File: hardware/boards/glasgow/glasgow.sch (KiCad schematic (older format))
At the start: 80 parts, among them J1 USB_B_Micro, U1 CY7C68013A-56LTX, U15 TPD3S014, U2 CAT24M01W, U3 CAT24C256W, U30 ICE40HX8K-BG121, U34 ATECC508A, U7 LM3880MF-1AF, U8 MIC5355-S4YMME, Y1 24M

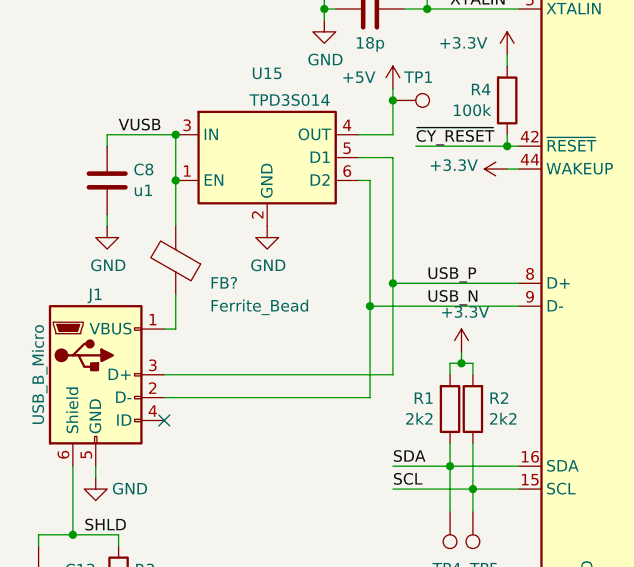
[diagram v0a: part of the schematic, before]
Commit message: Added 1BitSquared BOM keys to the schematic.
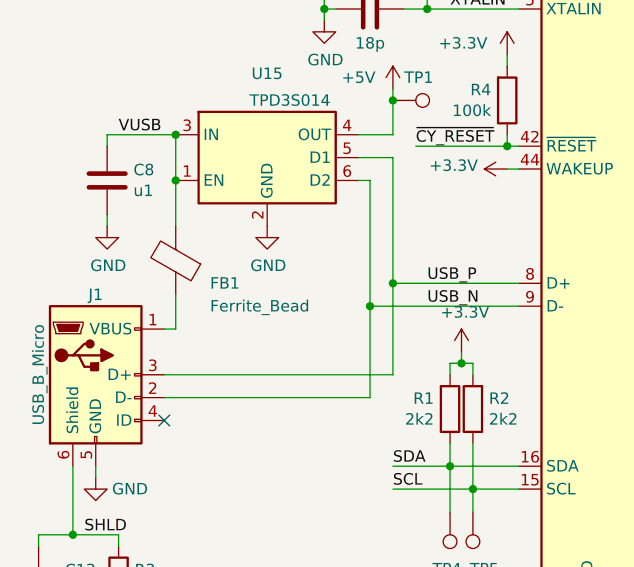
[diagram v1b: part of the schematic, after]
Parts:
- C1, C14, C19, C26, C27, C28, C76, C80: Key (none) -> cap-cer-0603-4u7
- C10, C13, C15, C16, C17, C18, C2, C20, C21, C23, C24, C25, C3, C4, C5, C6, C7, C77, C78, C79, C8, C81, C9: Key (none) -> cap-cer-0402-100n
- C11, C12: Key (none) -> cap-cer-0402-18p
- D1, D2, D3: Key (none) -> led-0603-grn
- D4: Key (none) -> led-0603-yel
- D5: Key (none) -> led-0603-red
- FB1: renamed from FB?; Key (none) -> ferrite-0402-600
- J1: Key (none) -> conn-smd-usb-micro-b
- R1, R12, R13, R14, R2: Key (none) -> res-0402-2k2
- R15: Key (none) -> res-0402-390
- R16: Key (none) -> res-0402-604
- R17, R18, R19, R4, R6, R7, R8, R9: Key (none) -> res-0402-100k
- R3: Key (none) -> res-0402-1m
- R31, R32: Key (none) -> res-0402-100
- R5: Key (none) -> res-0402-220k
- U1: Key (none) -> ic-cy7c68013a-56ltx
- U15: Key (none) -> ic-sot23-6-tpd3s014
- U2: Key (none) -> ic-soic8-cat24m01w
- U3: Key (none) -> ic-soic8-cat24c256w
- U30: Key (none) -> ic-ice40hx8k-bg121
- U34: Key (none) -> ic-wdfn8-atecc508a
- U7: Key (none) -> ic-sot23-6-lm3880mf-1af
- U8: Key (none) -> ic-msop8-mic5355-s4ymme
- Y1: Key (none) -> xtal-lfxtal-24mhz
